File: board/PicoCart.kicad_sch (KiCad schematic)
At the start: 29 parts, among them J1 MSX Bus (Odd-Even), J2 Micro_SD_Card, J3 UART, J4 DEBUG, J5 MSX Debug, J6 Pico Debug, J7 Ground Pins, J8 Ground Pins, J9 Edge Connector, U1 LD1117S33TR_SOT223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

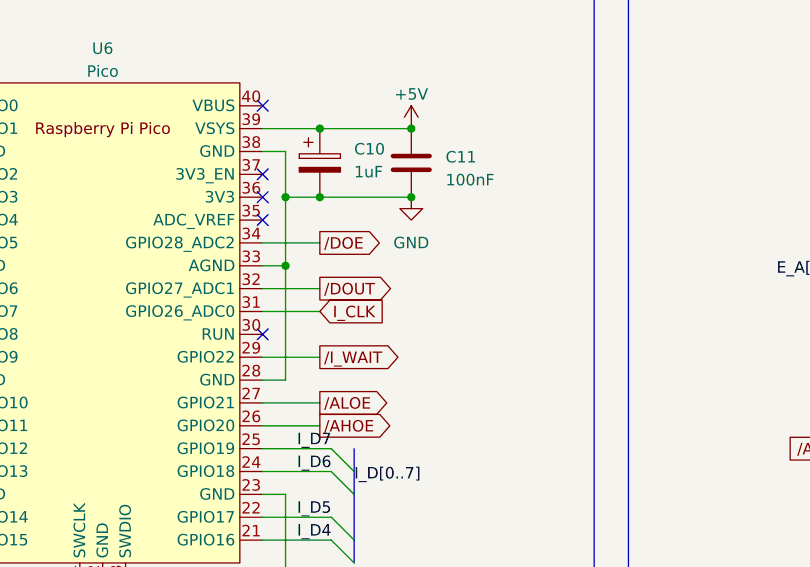
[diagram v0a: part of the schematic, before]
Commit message: Swapped DoE and IWait
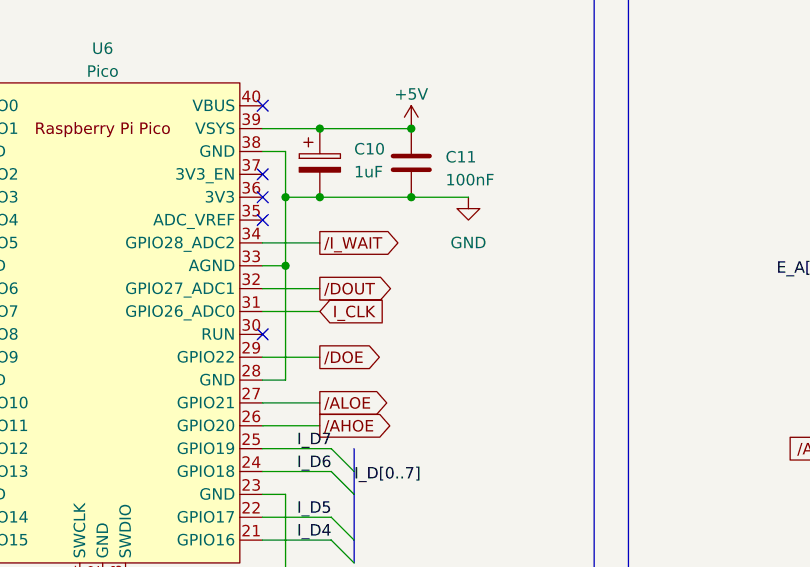
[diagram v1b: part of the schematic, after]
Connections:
- net /DOE: now also U6.29 (GPIO22); no longer U6.34 (GPIO28_ADC2)
- net /I_WAIT: now also U6.34 (GPIO28_ADC2); no longer U6.29 (GPIO22)
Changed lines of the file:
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@@
     (rev "2b")
     (company "NormStudios")
+    (comment 1 "2024-02-18 : Switched I_WAIT and I_DOE on Pi Pico")
   )
   (junction (at 339.09 99.06) (diameter 0) (color 0 0 0 0)
@@
     (stroke (width 0) (type default))
   )
+  (wire (pts (xy 102.87 66.04) (xy 96.52 66.04))
+    (stroke (width 0) (type default))
+  )
   (wire (pts (xy 382.27 160.02) (xy 382.27 162.56))
     (stroke (width 0) (type default))
@@
     )
   )
+  (global_label "{slash}DOE" (shape output) (at 86.36 83.82 0) (fields_autoplaced)
+    (effects (font (size 1.27 1.27)) (justify left))
+    (property "Intersheetrefs" "${INTERSHEET_REFS}" (at 94.3458 83.82 0)
+      (effects (font (size 1.27 1.27)) (justify left) hide)
+    )
+  )
   (global_label "{slash}DOUT" (shape input) (at 146.05 204.47 180) (fields_autoplaced)
     (effects (font (size 1.27 1.27)) (justify right))
@@
     )
   )
-  (global_label "{slash}I_WAIT" (shape output) (at 86.36 83.82 0) (fields_autoplaced)
-    (effects (font (size 1.27 1.27)) (justify left))
-    (property "Intersheetrefs" "${INTERSHEET_REFS}" (at 96.2811 83.82 0)
-      (effects (font (size 1.27 1.27)) (justify left) hide)
-    )
-  )
   (global_label "{slash}WAIT" (shape input) (at 240.03 54.61 180) (fields_autoplaced)
     (effects (font (size 1.27 1.27)) (justify right))
@@
     )
   )
-  (global_label "{slash}DOE" (shape output) (at 86.36 71.12 0) (fields_autoplaced)
-    (effects (font (size 1.27 1.27)) (justify left))
-    (property "Intersheetrefs" "${INTERSHEET_REFS}" (at 94.3458 71.12 0)
-      (effects (font (size 1.27 1.27)) (justify left) hide)
-    )
-  )
   (global_label "{slash}E_READ" (shape output) (at 273.05 62.23 0) (fields_autoplaced)
     (effects (font (size 1.27 1.27)) (justify left))
@@
     )
   )
+  (global_label "{slash}I_WAIT" (shape output) (at 86.36 71.12 0) (fields_autoplaced)
+    (effects (font (size 1.27 1.27)) (justify left))
+    (property "Intersheetrefs" "${INTERSHEET_REFS}" (at 96.2811 71.12 0)
+      (effects (font (size 1.27 1.27)) (justify left) hide)
+    )
+  )
   (global_label "{slash}E_SLTSEL" (shape output) (at 370.84 48.26 0) (fields_autoplaced)
     (effects (font (size 1.27 1.27)) (justify left))
@@
     )
   )
-  (symbol (lib_id "power:GND") (at 96.52 66.04 0) (unit 1)
+  (symbol (lib_id "power:GND") (at 102.87 66.04 0) (unit 1)
     (in_bom yes) (on_board yes) (dnp no) (fields_autoplaced)
-    (property "Reference" "#PWR036" (at 96.52 72.39 0)
+    (property "Reference" "#PWR036" (at 102.87 72.39 0)
       (effects (font (size 1.27 1.27)) hide)
     )
-    (property "Value" "GND" (at 96.52 71.12 0)
+    (property "Value" "GND" (at 102.87 71.12 0)
       (effects (font (size 1.27 1.27)))
     )
-    (property "Footprint" "" (at 96.52 66.04 0)
+    (property "Footprint" "" (at 102.87 66.04 0)
       (effects (font (size 1.27 1.27)) hide)
     )
-    (property "Datasheet" "" (at 96.52 66.04 0)
+    (property "Datasheet" "" (at 102.87 66.04 0)
       (effects (font (size 1.27 1.27)) hide)
     )
